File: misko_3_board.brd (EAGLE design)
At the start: 74 x 152 mm, 179 parts, among them IC1 ATMEGA1281-16AU, IC10 ORG1510-MK4, IC11 TPS3808G33DBVT, IC12 LTC4425, IC13 RN-42, IC14 ADXL345, IC15 74HCT1G32, IC16 FM25W256-SOIC, IC17 MICROSD_SPI_MODE, IC18 FH12-30S-0.5SH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

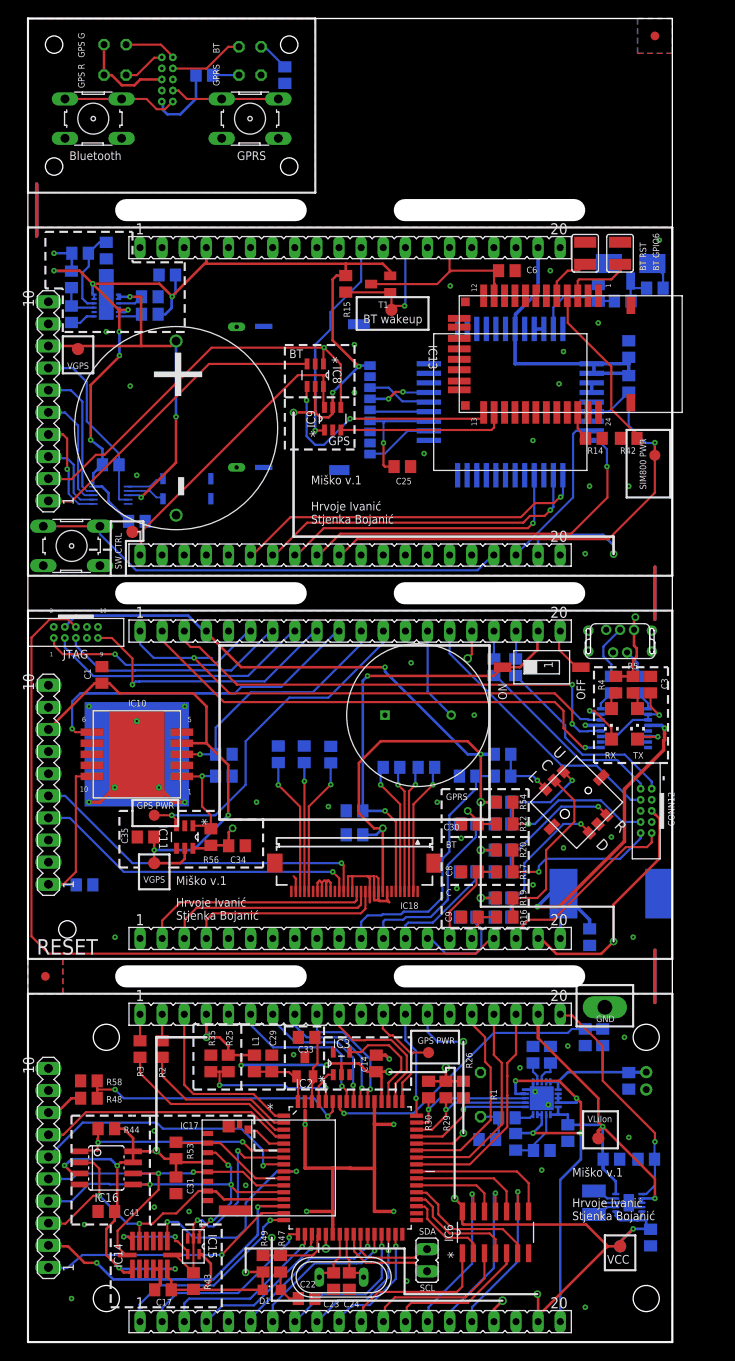
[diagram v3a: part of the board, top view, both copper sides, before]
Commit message: - corrected for larger holes on 1.27mm connectors - moved fiducials around - rerouted a few traces around the 1.27mm connectors - added milling around mini usb socket
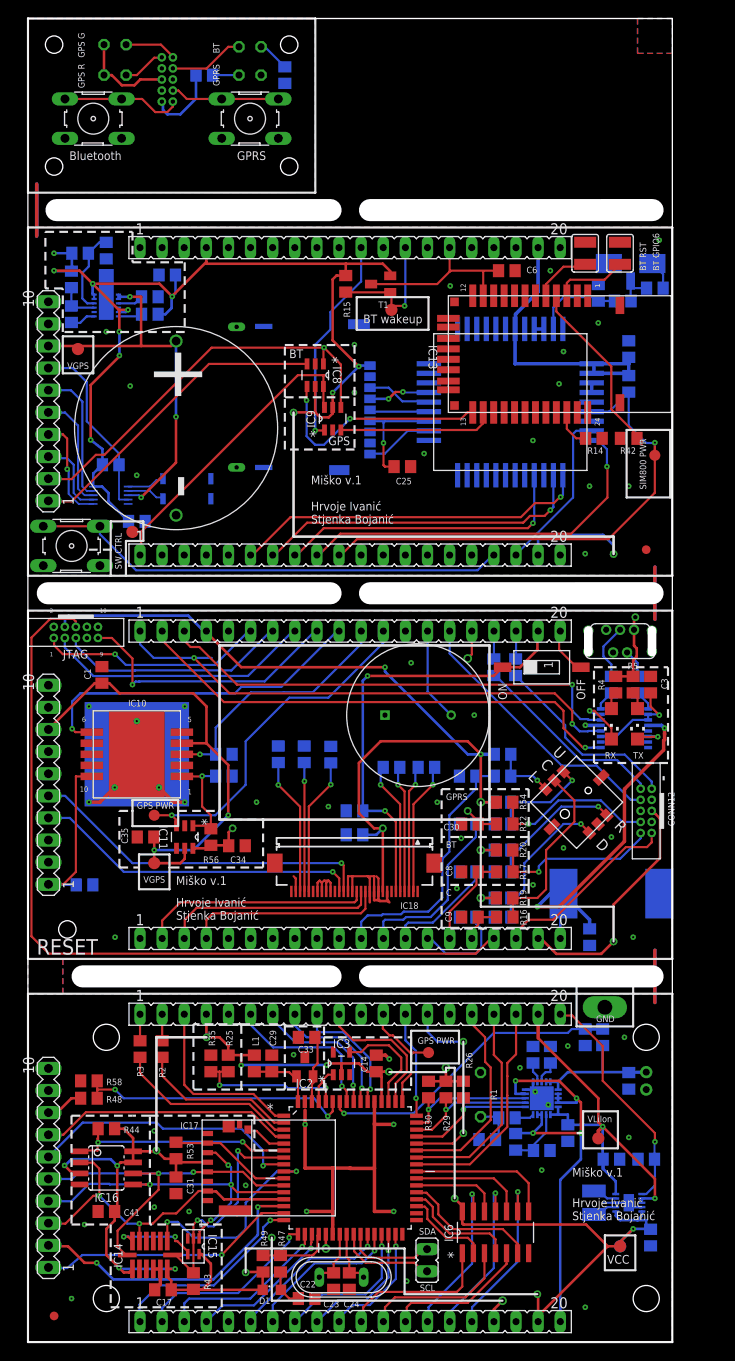
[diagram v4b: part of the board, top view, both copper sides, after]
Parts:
- CONN10: device JTAG 1.27mm 10pin header:TH-JTAG -> 1.27mm 10pin header:TH
- moved FI2 59.0 mm to (71.0, 91.0)
- moved FI1 39.0 mm to (3.00, 3.00)
- moved IC13 1.25 mm to (48.3, 120.2)
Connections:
- net GND: now also CONN10.10, CONN10.2; no longer CONN10.GND1, CONN10.GND2
- net JTAG_TCL_PIN: now also CONN10.1; no longer CONN10.TCK
- net JTAG_TDI_PIN: now also CONN10.9; no longer CONN10.TDI
- net JTAG_TDO_PIN: now also CONN10.3; no longer CONN10.TDO
- net JTAG_TMS_PIN: now also CONN10.5; no longer CONN10.TMS
- net RESET: now also CONN10.6; no longer CONN10.RESET
- net VCC: now also CONN10.4; no longer CONN10.VCC
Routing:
- net BLUE_LED: track 64.0 -> 61.1 mm
- net BLUETOOTH_TX: track 19.4 -> 17.9 mm
- net BLUETOOTH_RX: track 28.2 -> 26.8 mm
- net GPIO4: track 3.28 -> 4.50 mm
- net BT_RST: track 5.70 -> 6.78 mm
- net BUTTON_BLUETOOTH: track 33.0 -> 33.6 mm
- net VCC: track 456.7 -> 457.3 mm
- net GPIO7: track 19.7 -> 20.2 mm
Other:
- outline, holes or cut-outs redrawn

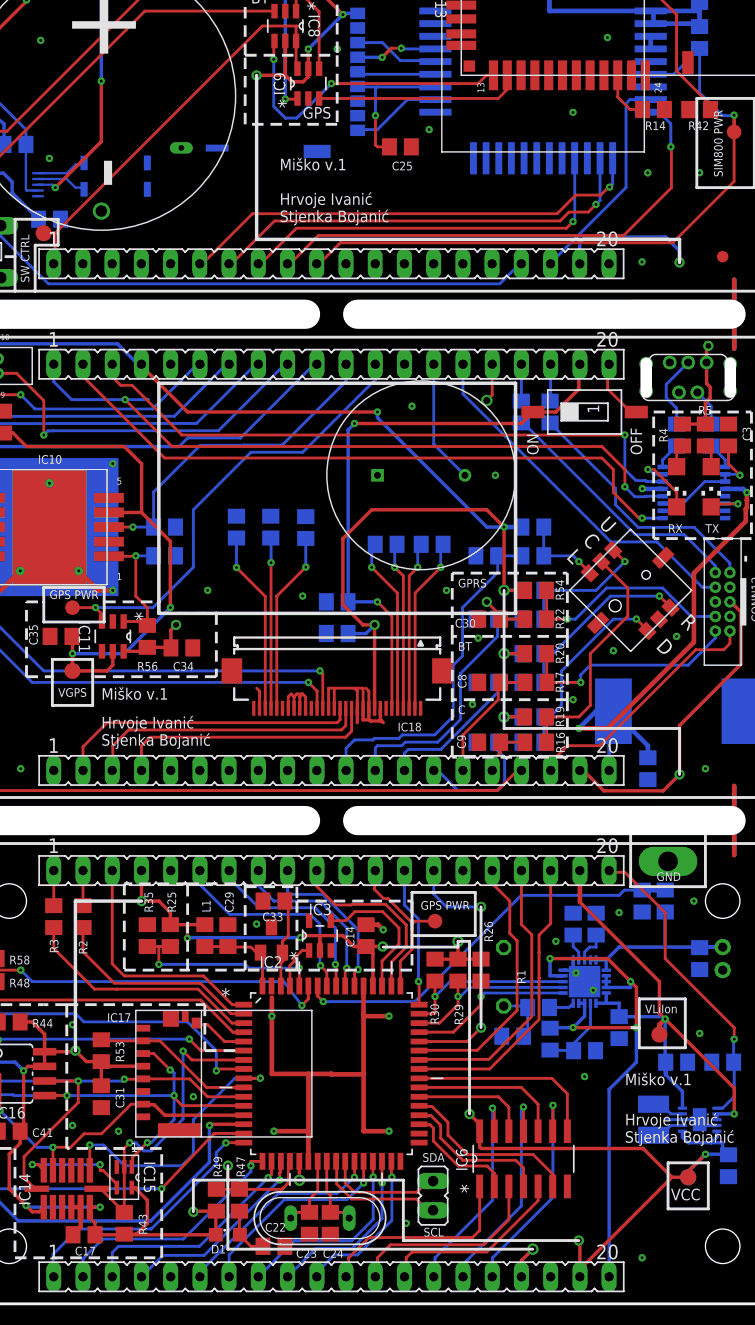
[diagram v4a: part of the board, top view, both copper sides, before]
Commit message: - made wire-connected holes/traces larger
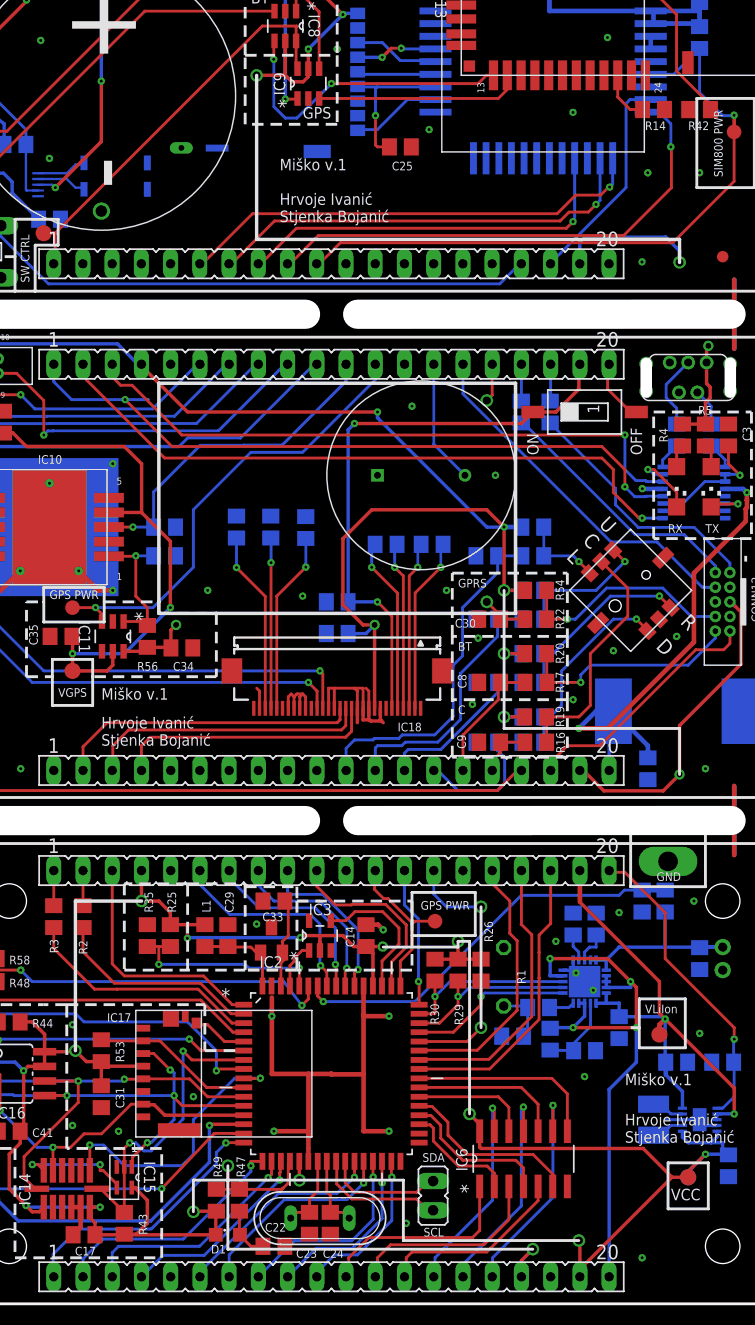
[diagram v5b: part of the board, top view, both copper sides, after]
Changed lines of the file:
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@@
 <wire x1="27" y1="8.05" x2="25.05" y2="8.05" width="0.3" layer="1"/>
 <wire x1="25.05" y1="8.05" x2="25" y2="8" width="0.3" layer="1"/>
-<via x="25" y="8" extent="1-16" drill="0.5" shape="octagon"/>
+<via x="25" y="8" extent="1-16" drill="0.7" shape="octagon"/>
 <wire x1="34.206" y1="12.38" x2="34.206" y2="11.0152" width="0.3" layer="1"/>
 <wire x1="34.206" y1="11.0152" x2="34.2212" y2="10.74" width="0.3" layer="1"/>
-<via x="34.2212" y="10.74" extent="1-16" drill="0.6" shape="octagon"/>
+<via x="34.2212" y="10.74" extent="1-16" drill="0.7" shape="octagon"/>
 <contactref element="IC20" pad="VCC"/>
 <wire x1="5.04" y1="123.04" x2="5.04" y2="125.04" width="0.3" layer="16"/>
@@
 <wire x1="49.88" y1="15.62" x2="49.88" y2="15" width="0.3" layer="1"/>
 <wire x1="49.88" y1="15.62" x2="49" y2="16.5" width="0.3" layer="1"/>
-<via x="49" y="16.5" extent="1-16" drill="0.5" shape="octagon"/>
+<via x="49" y="16.5" extent="1-16" drill="0.7" shape="octagon"/>
 <wire x1="70" y1="14" x2="71" y2="14" width="0.3" layer="16"/>
 <wire x1="71" y1="14" x2="71" y2="13.05" width="0.3" layer="16"/>
@@
 <via x="40.75" y="59" extent="1-16" drill="0.5" shape="octagon"/>
 <wire x1="53.55" y1="62" x2="52" y2="62" width="0.3" layer="16"/>
-<via x="52" y="62" extent="1-16" drill="0.6" shape="octagon"/>
+<via x="52" y="62" extent="1-16" drill="0.7" shape="octagon"/>
 <wire x1="52" y1="62" x2="53.79" y2="62" width="0.3" layer="1"/>
 <wire x1="53.55" y1="56.5" x2="52" y2="56.5" width="0.3" layer="16"/>
-<via x="52" y="56.5" extent="1-16" drill="0.6" shape="octagon"/>
+<via x="52" y="56.5" extent="1-16" drill="0.7" shape="octagon"/>
 <wire x1="52" y1="56.5" x2="53.79" y2="56.5" width="0.3" layer="1"/>
 <wire x1="53.55" y1="51" x2="52" y2="51" width="0.3" layer="16"/>
-<via x="52" y="51" extent="1-16" drill="0.6" shape="octagon"/>
+<via x="52" y="51" extent="1-16" drill="0.7" shape="octagon"/>
 <wire x1="52" y1="51" x2="53.79" y2="51" width="0.3" layer="1"/>
 <wire x1="20.49" y1="81.65" x2="20.49" y2="81.51" width="0.4064" layer="1"/>
@@
 <via x="10.25" y="20.25" extent="1-16" drill="0.25"/>
 <wire x1="48" y1="29.95" x2="48" y2="31.5" width="0.3" layer="1"/>
-<via x="48" y="31.5" extent="1-16" drill="0.6" shape="octagon"/>
+<via x="48" y="31.5" extent="1-16" drill="0.7" shape="octagon"/>
 <wire x1="36" y1="30.7046" x2="36" y2="32" width="0.3" layer="1"/>
 <wire x1="9.95" y1="13.95" x2="9.95" y2="15" width="0.3048" layer="1"/>
@@
 <wire x1="58.59" y1="2.35" x2="58.59" y2="5.41" width="0.3" layer="1"/>
 <wire x1="58.59" y1="5.41" x2="58.5" y2="5.5" width="0.3" layer="1"/>
-<via x="58.5" y="5.5" extent="1-16" drill="0.5" shape="octagon"/>
+<via x="58.5" y="5.5" extent="1-16" drill="0.7" shape="octagon"/>
 <wire x1="20.49" y1="37.65" x2="20.49" y2="35.01" width="0.3" layer="1"/>
 <wire x1="20.49" y1="35.01" x2="20.5" y2="35" width="0.3" layer="1"/>
-<via x="20.5" y="35" extent="1-16" drill="0.5" shape="octagon"/>
+<via x="20.5" y="35" extent="1-16" drill="0.7" shape="octagon"/>
 <wire x1="23" y1="32.95" x2="23" y2="33.25" width="0.3" layer="1"/>
 <wire x1="23" y1="34" x2="23" y2="32.95" width="0.3" layer="1"/>
 <wire x1="20.5" y1="35" x2="22" y2="35" width="0.3" layer="1"/>
 <wire x1="22" y1="35" x2="23" y2="34" width="0.3" layer="1"/>
-<via x="14.75" y="22" extent="1-16" drill="0.5" shape="octagon"/>
+<via x="14.75" y="22" extent="1-16" drill="0.7" shape="octagon"/>
 <wire x1="12.0734" y1="21.905" x2="14.655" y2="21.905" width="0.3" layer="1"/>
 <wire x1="14.75" y1="22" x2="14.655" y2="21.905" width="0.3" layer="1"/>
@@
 <wire x1="32.99" y1="106.76560625" x2="30.51560625" y2="106.76560625" width="0.3" layer="1"/>
 <wire x1="30.51560625" y1="106.76560625" x2="30.5" y2="106.75" width="0.3" layer="1"/>
-<via x="30.5" y="106.75" extent="1-16" drill="0.5" shape="octagon"/>
-<via x="67.25" y="90.5" extent="1-16" drill="0.5" shape="octagon"/>
+<via x="30.5" y="106.75" extent="1-16" drill="0.7" shape="octagon"/>
+<via x="67.25" y="90.5" extent="1-16" drill="0.7" shape="octagon"/>
 <wire x1="58.58" y1="90.38" x2="58.58" y2="92.2375375" width="0.3" layer="16"/>
 <wire x1="58.58" y1="92.2375375" x2="59.04623125" y2="92.70376875" width="0.3" layer="16"/>
@@
 <contactref element="CONN6" pad="17"/>
 <contactref element="CONN9" pad="17"/>
-<via x="54.5" y="4.75" extent="1-16" drill="0.6" shape="octagon"/>
+<via x="54.5" y="4.75" extent="1-16" drill="0.7" shape="octagon"/>
 <wire x1="1.7588" y1="93.6906" x2="8.2612" y2="93.6906" width="0.25" layer="1"/>
 <wire x1="32.3" y1="9.95" x2="32.683275" y2="9.95" width="0.25" layer="1"/>
@@
 <wire x1="27" y1="9.95" x2="29" y2="9.95" width="0.25" layer="1"/>
 <wire x1="28" y1="9.95" x2="28" y2="12" width="0.25" layer="1"/>
-<via x="28" y="12" extent="1-16" drill="0.5"/>
+<via x="28" y="12" extent="1-16" drill="0.7"/>
 <wire x1="53.51" y1="46.35" x2="53.1653875" y2="46.35" width="0.25" layer="1"/>
 <wire x1="53.1653875" y1="46.35" x2="51.4195875" y2="44.6042" width="0.25" layer="1"/>
@@
 <wire x1="50.97" y1="81.65" x2="50.97" y2="78.97" width="0.25" layer="1"/>
 <wire x1="50.97" y1="78.97" x2="50.5" y2="78.5" width="0.25" layer="1"/>
-<via x="50.5" y="78.5" extent="1-16" drill="0.6"/>
+<via x="50.5" y="78.5" extent="1-16" drill="0.7"/>
 <wire x1="44.62" y1="22.0066" x2="44.6474" y2="22.034" width="0.25" layer="1"/>
 <wire x1="53.1364" y1="31.54314375" x2="52.5" y2="32.17954375" width="0.25" layer="1"/>
@@
 <wire x1="51.7" y1="59.8" x2="51.7" y2="59.5" width="0.25" layer="1"/>
 <wire x1="51.7" y1="59.8" x2="50.5" y2="61" width="0.25" layer="1"/>
-<via x="50.5" y="61" extent="1-16" drill="0.5"/>
+<via x="50.5" y="61" extent="1-16" drill="0.7"/>
 <wire x1="51.7" y1="59.5" x2="53.8" y2="59.5" width="0.25" layer="1"/>
 <wire x1="50.97" y1="81.65" x2="50.96" y2="125.69" width="0" layer="19" extent="1-1"/>
@@
 <wire x1="99" y1="45.43" x2="111" y2="45.43" width="0" layer="19" extent="1-1"/>
 <wire x1="72" y1="45" x2="99" y2="45.43" width="0" layer="19" extent="16-16"/>
-<wire x1="49.55" y1="48.8" x2="49.8" y2="48.8" width="0" layer="19" extent="1-16"/>
 <wire x1="49.55" y1="59.5" x2="49.8" y2="59.5" width="0" layer="19" extent="1-16"/>
 <wire x1="59" y1="28" x2="59.75" y2="27.25" width="0" layer="19" extent="16-16"/>
+<wire x1="49.55" y1="48.8" x2="49.25" y2="52.1" width="0" layer="19" extent="16-16"/>
+<wire x1="49.8" y1="48.8" x2="49.55" y2="48.8" width="0" layer="19" extent="1-16"/>
 </signal>
 <signal name="GPRS_LED" class="2">
@@
 <wire x1="44.62" y1="22.794" x2="48.794" y2="22.794" width="0.25" layer="1"/>
 <wire x1="48.794" y1="22.794" x2="50" y2="24" width="0.25" layer="1"/>
-<via x="50" y="24" extent="1-16" drill="0.5"/>
+<via x="50" y="24" extent="1-16" drill="0.7"/>
 <contactref element="U$1" pad="SIGNAL"/>
 <wire x1="45.89" y1="81.65" x2="45.89" y2="74.71" width="0.25" layer="16"/>
@@
 <wire x1="45.89" y1="35.61" x2="47" y2="34.5" width="0.25" layer="16"/>
 <wire x1="47" y1="34.5" x2="50" y2="34.5" width="0.25" layer="16"/>
-<via x="50" y="34.5" extent="1-16" drill="0.5"/>
+<via x="50" y="34.5" extent="1-16" drill="0.7"/>
 <wire x1="45.89" y1="81.65" x2="45.88" y2="125.69" width="0" layer="19" extent="1-1"/>
 <wire x1="45.89" y1="37.65" x2="48.6" y2="72" width="0" layer="19" extent="1-1"/>

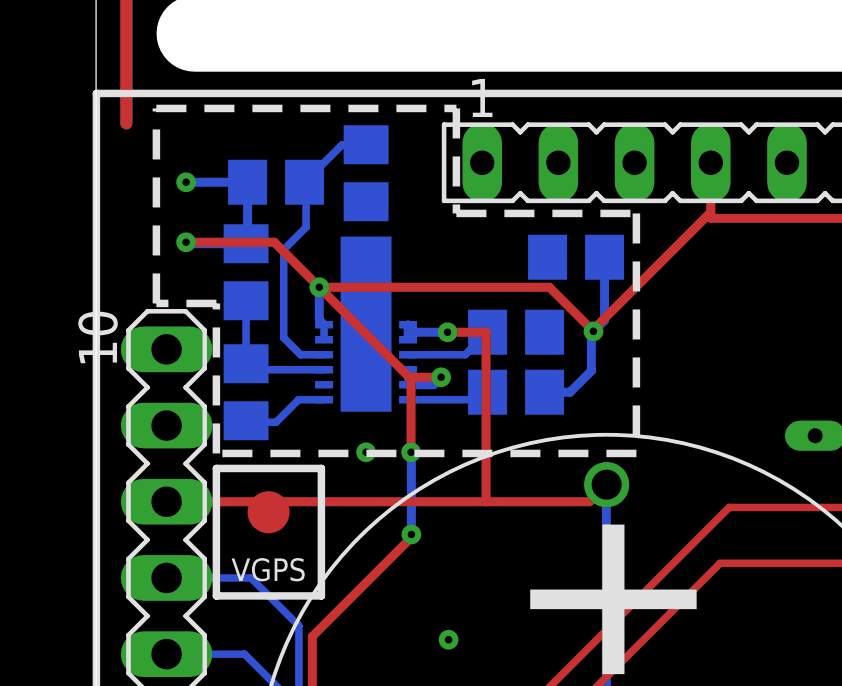
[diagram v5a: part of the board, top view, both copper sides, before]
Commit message: - corrected wrong layout for ltc4425, updated gerber files
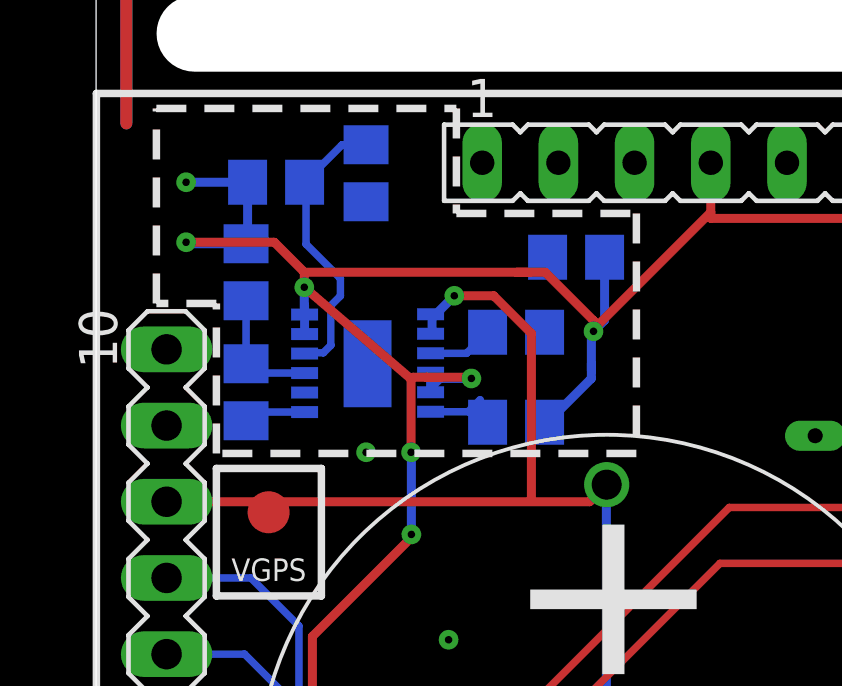
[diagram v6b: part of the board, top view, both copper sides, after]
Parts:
- IC12: device LTC4425 Supercap Charger:DFN12 -> LTC4425 Supercap Charger:MSOP
- moved R39 1.00 mm to (14.0, 117.0)
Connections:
- net VCC: now also IC12.VIN1, IC12.VIN2; no longer IC12.VCC1, IC12.VCC2
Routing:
- net VCC: track 457.3 -> 462.2 mm
- net VGPS: track 105.6 -> 107.3 mm
- net PFI_RET: track 2.93 -> 2.07 mm
- net LTC4425_PROG: track 2.96 -> 2.19 mm
- net PFI: track 4.78 -> 4.18 mm
